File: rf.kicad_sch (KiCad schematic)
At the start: 7 parts, among them U3 MAX-M10S, Y1 ECS-TXO-25CSMV-320-AM-TR

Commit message: oops forgot to commit - looks like I worked on the lr2021's symbol and the schematic - see journal for details on what I did
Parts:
- added C20: 47pF, symbol Device:C
- added C24: 22pF, symbol Device:C
- added C27: 7.5pF, symbol Device:C
- added C28, C30: 1.8pF, symbol Device:C
- added C29: 3.9pF, symbol Device:C
- added C31: 4.7uF, symbol Device:C
- added C32: 2.2pF, symbol Device:C
- added C33: 18pF, symbol Device:C
- added C34, C35: 1uF, symbol Device:C
- added C36, C37: 2.2uF, symbol Device:C
- added J10: UFL, symbol Connector:Conn_Coaxial
- added L3: 12nH, symbol Device:L
- added L4: 4.7nH, symbol Device:L
- added L5: 3.9nH, symbol Device:L
- added L6: 7.5nH, symbol Device:L
- added L7: 22nH, symbol Device:L
- added L8: 24nH, symbol Device:L
- C14: value C -> 100nF
- L2: value L -> 2.2uH
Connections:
- net +3.3V: now also C14.1, LR1.12 (VDCC1), LR1.13 (VPAX1), LR1.17 (VBAT), LR1.2 (VPAX2), LR1.26 (VDCC2), C31.1, C34.1, C35.1, C36.1, C37.2
- net GND: now also LR1.15 (GND_DCC), LR1.30 (GND), C20.2, C27.1, C29.1, C30.1, C31.2, C32.2, C34.2, C35.2, C36.2, C37.1, J10.2 (Ext), L7.1
- net spi_miso: now also LR1.21 (MISO); no longer LR1. (NSS)
- net spi_mosi: now also LR1.22 (MOSI); no longer LR1. (NSS)
- net spi_nss: now also LR1.24 (NSS); no longer LR1. (NSS)
- net spi_sclk: now also LR1.23 (SCK); no longer LR1. (NSS)
- net telem_busy: now also LR1.25 (BUSY); no longer LR1. (NSS)
- net telem_rst: now also LR1.20 (NRST); no longer LR1. (NSS)
- net at Y1.3 (OUTPUT): now also LR1.4 (XTA); no longer LR1. (NSS)
- net at Y1.4 (VDD): now also LR1.6 (VTCXO/VNTC); no longer LR1. (NSS)
- net at L2.1: now also LR1.14 (LXB); no longer LR1. (NSS)
- new net: C30.2, C33.2, J10.1 (In), L6.2, L7.2
- new net: C24.1, L4.2
- new net: C24.2, C27.2, C28.1, L5.1
- new net: L3.2, L4.1, LR1.27 (RFO_LF2), LR1.28 (RFO_LF1)
- new net: C28.2, C29.2, L5.2, L6.1
- new net: C32.1, C33.1, L8.2
- new net: L8.1, LR1.29 (RFI_LF)
- new net: L2.2, LR1.16 (LXA)
- new net vr_pa: C20.1, L3.1, LR1.1 (VR_PA)
- no-connect marks 15 -> 17
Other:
- moved on the sheet: L2

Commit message: tons of progress on schematic and pcb - see journal for details
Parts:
- C25: renamed from C37; footprint (none) -> Capacitor_SMD:C_0603_1608Metric
- C26: renamed from C20; footprint (none) -> Capacitor_SMD:C_0402_1005Metric
- C27, C32, C33: footprint (none) -> Capacitor_SMD:C_0402_1005Metric
- C28: renamed from C29; footprint (none) -> Capacitor_SMD:C_0402_1005Metric
- C29: renamed from C30; footprint (none) -> Capacitor_SMD:C_0402_1005Metric
- C30: renamed from C24; footprint (none) -> Capacitor_SMD:C_0402_1005Metric
- C31: renamed from C28; footprint (none) -> Capacitor_SMD:C_0402_1005Metric
- C34, C35: footprint (none) -> Capacitor_SMD:C_0603_1608Metric
- C36: renamed from C14; footprint (none) -> Capacitor_SMD:C_0402_1005Metric
- C37: renamed from C36; footprint (none) -> Capacitor_SMD:C_0603_1608Metric
- C38: renamed from C31; footprint (none) -> Capacitor_SMD:C_0603_1608Metric
- L2: renamed from L3; footprint (none) -> Inductor_SMD:L_0402_1005Metric
- L3: renamed from L7; footprint (none) -> Inductor_SMD:L_0402_1005Metric
- L4, L5, L6: footprint (none) -> Inductor_SMD:L_0402_1005Metric
- L7: renamed from L8; footprint (none) -> Inductor_SMD:L_0402_1005Metric
- L8: renamed from L2; footprint (none) -> Inductor_SMD:L_0402_1005Metric
- LR1: footprint (none) -> footprints:Untitled
- Y3: renamed from Y1; footprint ECSTXO25CSMV320AMTR -> footprints:ECSTXO25CSMV320AMTR
- renumbered C18 to C39, C17 to C40, U3 to U4
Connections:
- net spi_nss is gone; now on net GND: LR1.24 (NSS)

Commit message: worked mainly on pcb
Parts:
- removed J10: UFL, symbol Connector:Conn_Coaxial
- added C50, C51: C, Capacitor_SMD:C_0402_1005Metric, symbol Device:C
- added J10, J12: 73412-0114, footprints:73412-0110, symbol 73412-0114:73412-0114
- added L9: L, Inductor_SMD:L_0402_1005Metric, symbol Device:L
- C40: value 0.1uF -> 100nF
- L2: footprint Inductor_SMD:L_0402_1005Metric -> Inductor_SMD:L_0603_1608Metric
- L8: footprint Inductor_SMD:L_0402_1005Metric -> Inductor_SMD:L_0805_2012Metric
- LR1: footprint footprints:Untitled -> footprints:LR2021
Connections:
- net GND: now also LR1.0 (GND), C50.2, C51.2, J10.2 (GND_1), J10.3 (GND_2), J10.4 (GND_3), J12.2 (GND_1), J12.3 (GND_2), J12.4 (GND_3); no longer LR1. (GND)
- net at C29.2, C33.2, L3.2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: now also J10.1 (SIGNAL)
- net at U4.11 (RF_IN): now also C50.1, L9.2
- new net: C51.1, J12.1 (SIGNAL), L9.1

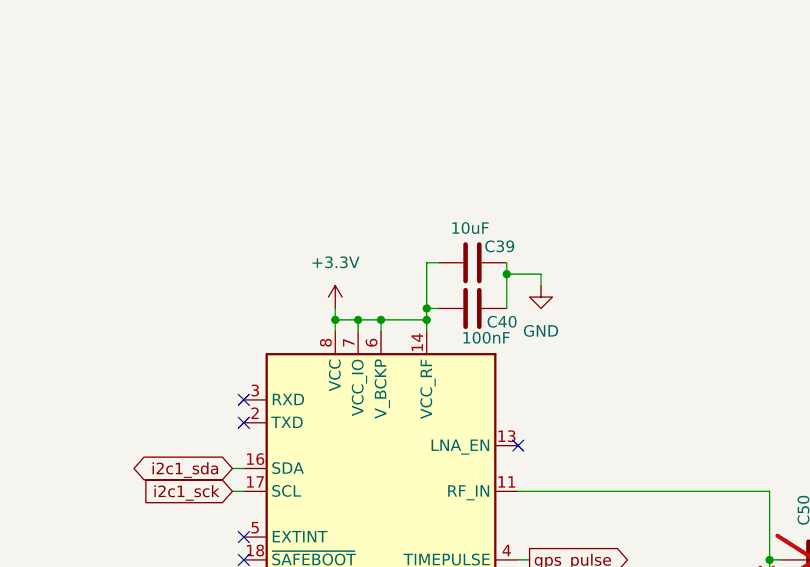
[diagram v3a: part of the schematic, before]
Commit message: basically just decoupling capacitors that I forgot
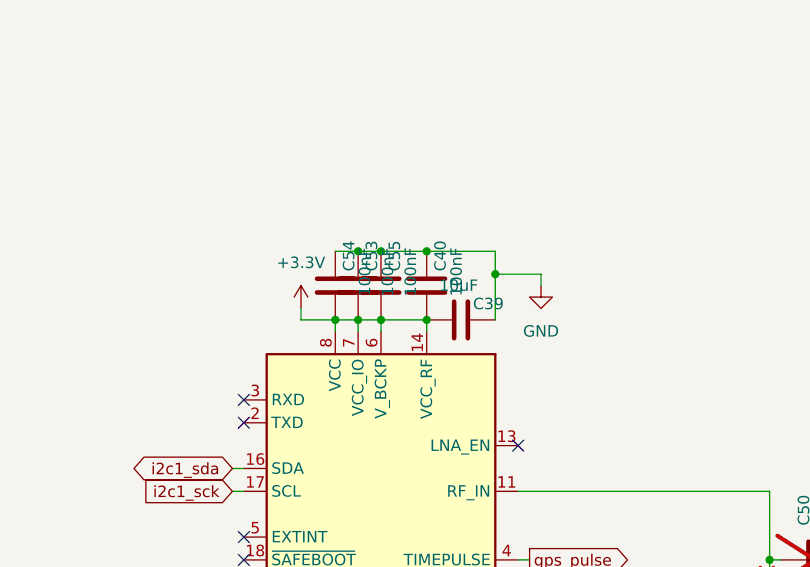
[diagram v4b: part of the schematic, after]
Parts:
- added C53, C54, C55: 100nF, Capacitor_SMD:C_0402_1005Metric, symbol Device:C
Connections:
- net +3.3V: now also C53.1, C54.1, C55.1
- net GND: now also C53.2, C54.2, C55.2
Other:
- moved on the sheet: C39, C40

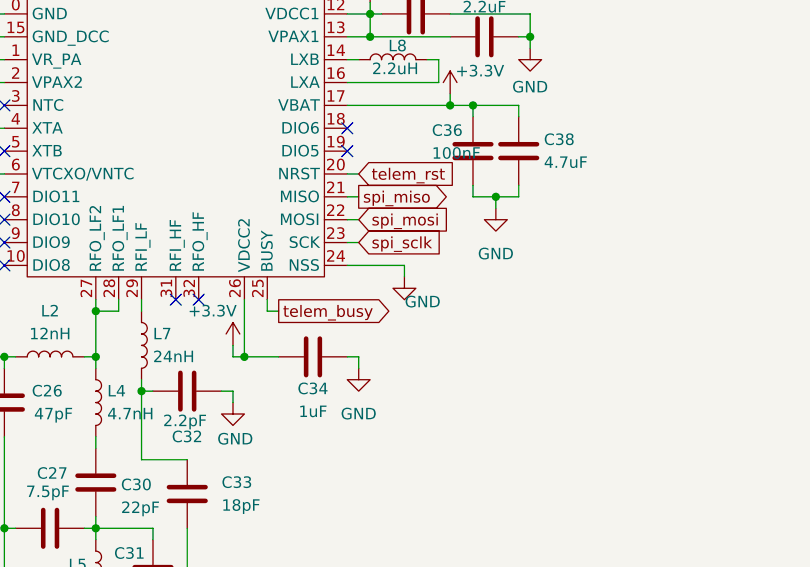
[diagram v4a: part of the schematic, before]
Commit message: added in the flash chip and micro sd card, rerouted some stuff, looking real nice rn - still need to finish rf, pyros, and add in the piezo
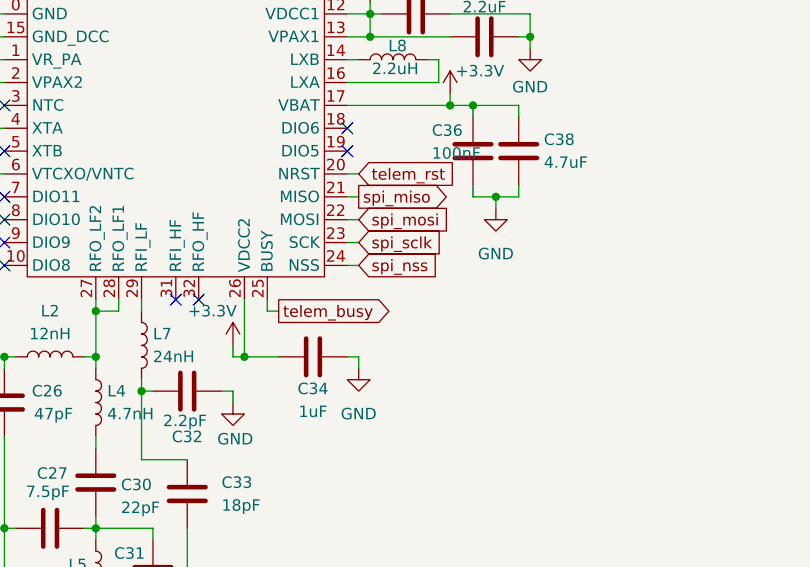
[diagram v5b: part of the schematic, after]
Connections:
- net GND: no longer LR1.24 (NSS)
- new net spi_nss: LR1.24 (NSS)
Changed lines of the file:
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@@
 	(wire
 		(pts
+			(xy 130.81 82.55) (xy 132.08 82.55)
+		)
+		(stroke
+			(width 0)
+			(type default)
+		)
+	)
+	(wire
+		(pts
 			(xy 257.81 99.06) (xy 229.87 99.06)
 		)
@@
 	(wire
 		(pts
-			(xy 130.81 82.55) (xy 137.16 82.55)
-		)
-		(stroke
-			(width 0)
-			(type default)
-		)
-	)
-	(wire
-		(pts
 			(xy 219.71 81.28) (xy 219.71 80.01)
 		)
@@
 		)
 	)
-	(wire
-		(pts
-			(xy 137.16 83.82) (xy 137.16 82.55)
-		)
-		(stroke
-			(width 0)
-			(type default)
-		)
-	)
 	(global_label "vr_pa"
 		(shape input)
@@
 		)
 	)
+	(global_label "spi_nss"
+		(shape input)
+		(at 132.08 82.55 0)
+		(fields_autoplaced yes)
+		(effects
+			(font
+				(size 1.27 1.27)
+			)
+			(justify left)
+		)
+		(property "Intersheetrefs" "${INTERSHEET_REFS}"
+			(at 142.0199 82.55 0)
+			(effects
+				(font
+					(size 1.27 1.27)
+				)
+				(justify left)
+				(hide yes)
+			)
+		)
+	)
 	(global_label "telem_rst"
 		(shape input)
@@
 					(unit 1)
 				)
-			)
-		)
-	)
-	(symbol
-		(lib_id "power:GND")
-		(at 137.16 83.82 0)
-		(unit 1)
-		(exclude_from_sim no)
-		(in_bom yes)
-		(on_board yes)
-		(dnp no)
-		(property "Reference" "#PWR076"
-			(at 137.16 90.17 0)
-			(effects
-				(font
-					(size 1.27 1.27)
-				)
-				(hide yes)
-			)
-		)
-		(property "Value" "GND"
-			(at 139.192 86.614 0)
-			(effects
-				(font
-					(size 1.27 1.27)
-				)
-			)
-		)
-		(property "Footprint" ""
-			(at 137.16 83.82 0)
-			(effects
-				(font
-					(size 1.27 1.27)
-				)
-				(hide yes)
-			)
-		)
-		(property "Datasheet" ""
-			(at 137.16 83.82 0)
-			(effects
-				(font
-					(size 1.27 1.27)
-				)
-				(hide yes)
-			)
-		)
-		(property "Description" "Power symbol creates a global label with name \"GND\" , ground"
-			(at 137.16 83.82 0)
-			(effects
-				(font
-					(size 1.27 1.27)
-				)
-				(hide yes)
-			)
-		)
-		(pin "1"
-		)
-		(instances
-			(project ""
-				(path "/d0cafa98-cc2a-4ab3-8dbc-f937bedf434b/370f9b44-a297-4225-a26d-62410af8a696"
-					(reference "#PWR076")
-					(unit 1)
-				)

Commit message: almost done routing! getting pretty close to done now
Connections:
- net gps_int: now reaches U4.5 (EXTINT)
- no-connect marks 17 -> 16
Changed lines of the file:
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@@
-	)
-	(no_connect
-		(at 199.39 104.14)
 	)
 	(no_connect
@@
 		(pts
 			(xy 102.87 123.19) (xy 102.87 124.46)
+		)
+		(stroke
+			(width 0)
+			(type default)
+		)
+	)
+	(wire
+		(pts
+			(xy 198.12 104.14) (xy 199.39 104.14)
 		)
 		(stroke
@@
 			(effects
 				(font
+					(size 1.27 1.27)
+				)
+				(justify right)
+				(hide yes)
+			)
+		)
+	)
+	(global_label "gps_int"
+		(shape output)
+		(at 198.12 104.14 180)
+		(fields_autoplaced yes)
+		(effects
+			(font
+				(size 1.27 1.27)
+			)
+			(justify right)
+		)
+		(property "Intersheetrefs" "${INTERSHEET_REFS}"
+			(at 188.3616 104.14 0)
+			(effects
+				(font

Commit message: schematic updated - need to redo the layout now
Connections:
- net gps_pulse: no longer names the net of U4.4 (TIMEPULSE)
- no-connect marks 16 -> 17

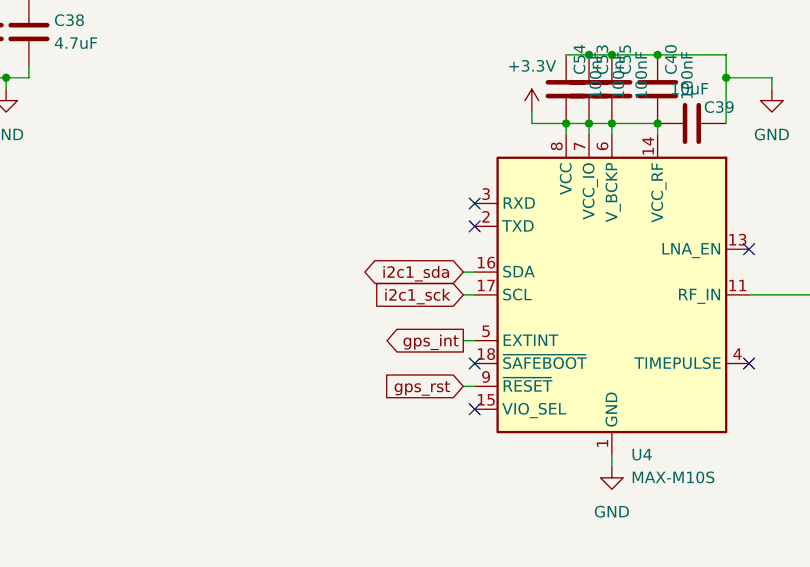
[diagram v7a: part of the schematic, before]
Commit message: started redoing layout for new pinout
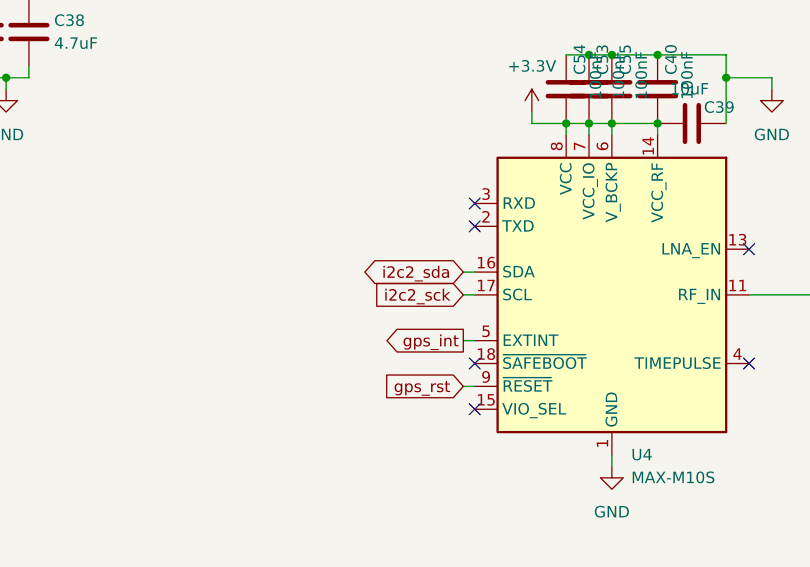
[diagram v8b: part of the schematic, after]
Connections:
- net i2c1_sck renamed i2c2_sck
- net i2c1_sda renamed i2c2_sda
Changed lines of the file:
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@@
 		)
 	)
-	(global_label "i2c1_sck"
+	(global_label "i2c2_sck"
 		(shape input)
 		(at 198.12 99.06 180)
@@
 		)
 	)
-	(global_label "i2c1_sda"
+	(global_label "i2c2_sda"
 		(shape bidirectional)
 		(at 198.12 96.52 180)
